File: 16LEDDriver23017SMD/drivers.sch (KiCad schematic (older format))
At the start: 80 parts, among them Q1 BC848, Q10 BC848, Q11 BC848, Q12 BC848, Q13 BC848, Q14 BC848, Q15 BC848, Q16 BC848, Q2 BC848, Q3 BC848, Q4 BC848, Q5 BC848, Q6 BC848, Q7 BC848, Q8 BC848, Q9 BC848

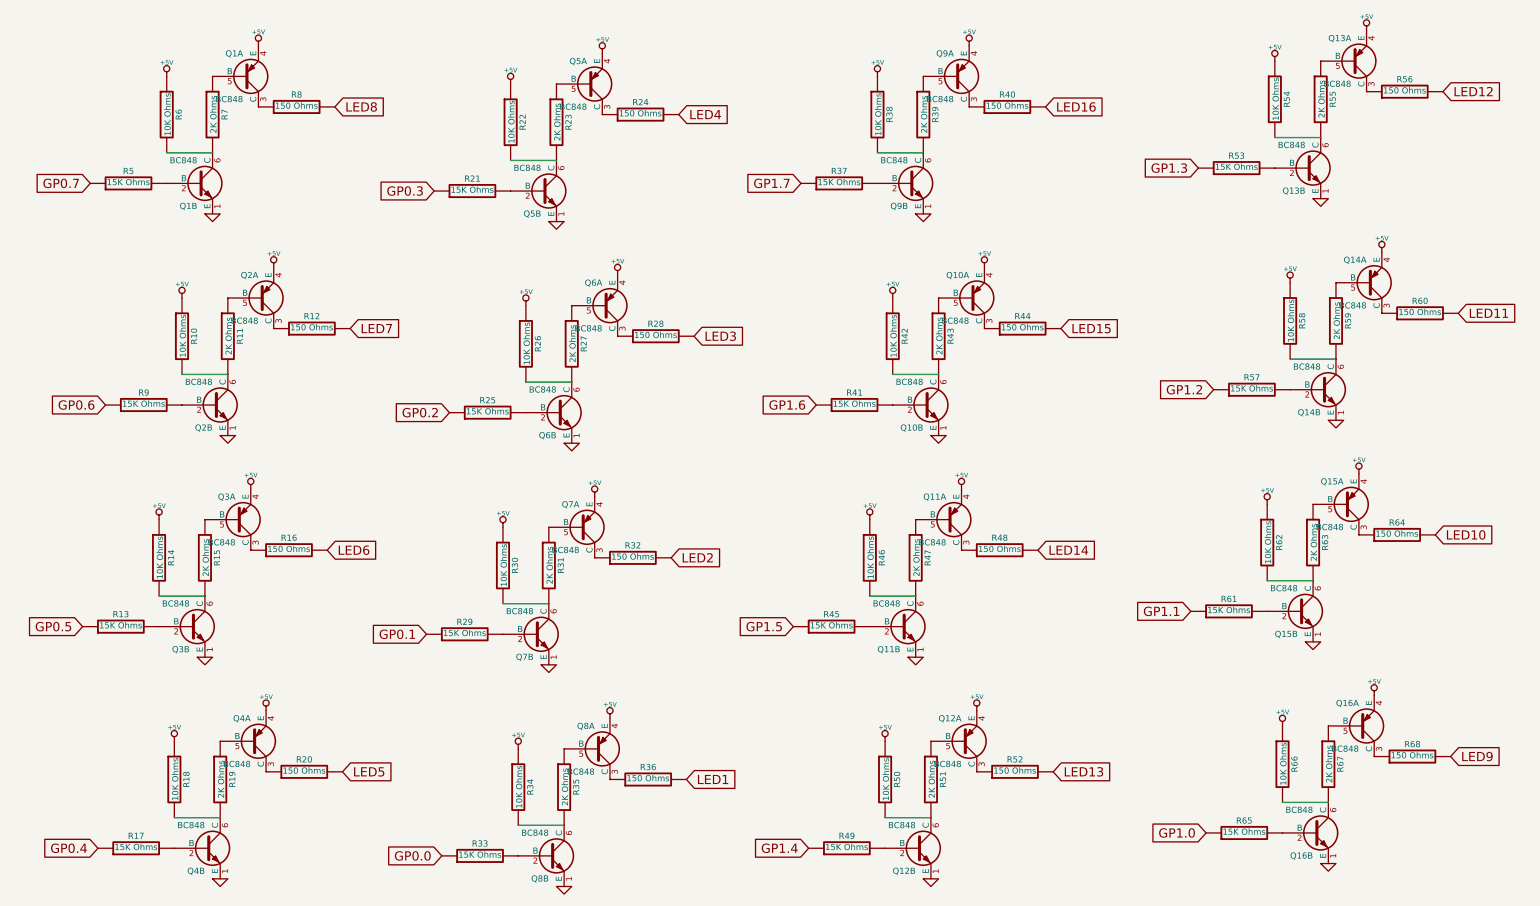
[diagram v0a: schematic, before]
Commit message: Shorten resistor values (remove " Ohms") to better fit the silk screen.
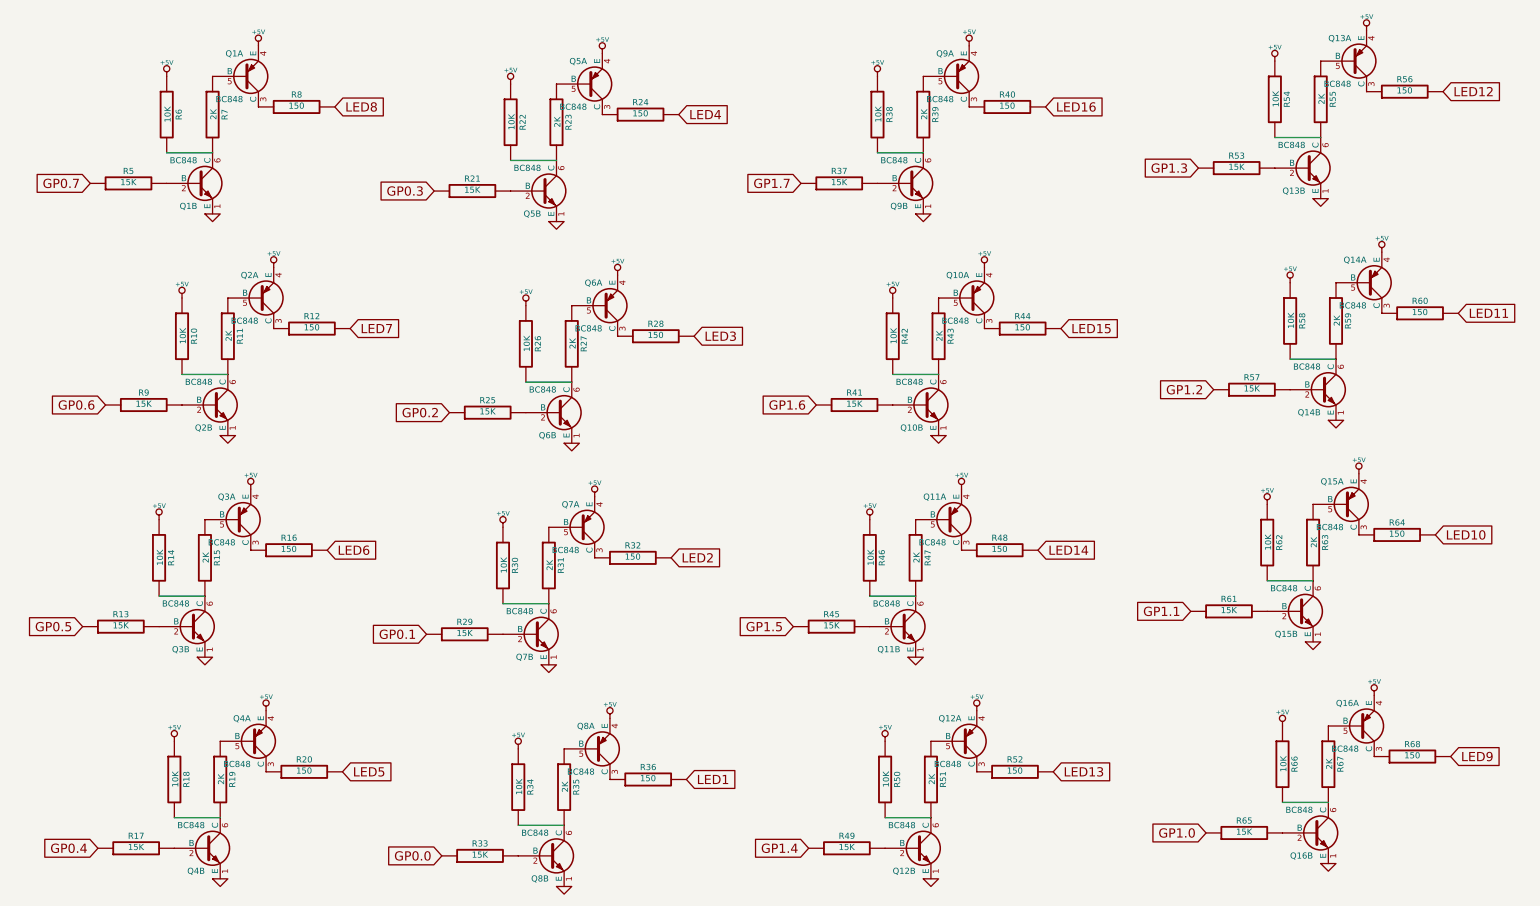
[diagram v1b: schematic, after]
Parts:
- R10, R14, R18, R22, R26, R30, R34, R38, R42, R46, R50, R54, R58, R6, R62, R66: value 10K Ohms -> 10K
- R11, R15, R19, R23, R27, R31, R35, R39, R43, R47, R51, R55, R59, R63, R67, R7: value 2K Ohms -> 2K
- R12, R16, R20, R24, R28, R32, R36, R40, R44, R48, R52, R56, R60, R64, R68, R8: value 150 Ohms -> 150
- R13, R17, R21, R25, R29, R33, R37, R41, R45, R49, R5, R53, R57, R61, R65, R9: value 15K Ohms -> 15K
